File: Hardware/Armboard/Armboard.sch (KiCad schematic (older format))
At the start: 12 parts

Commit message: H-Bridge completed
Completed the H-Bridge Hierarchal Sheet
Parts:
- Conn? (x12): symbol Armboard-rescue:AndersonPP-MRDT_Connectors-Armboard-rescue -> Armboard-rescue:AndersonPP-MRDT_Connectors-Armboard-rescue-Armboard-rescue
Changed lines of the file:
@@
 $EndSheet
 $Comp
-L Armboard-rescue:AndersonPP-MRDT_Connectors-Armboard-rescue Conn?
+L Armboard-rescue:AndersonPP-MRDT_Connectors-Armboard-rescue-Armboard-rescue Conn?
 U 3 1 5F73C0FD
 P 1140 1360
@@
 $EndComp
 $Comp
-L Armboard-rescue:AndersonPP-MRDT_Connectors-Armboard-rescue Conn?
+L Armboard-rescue:AndersonPP-MRDT_Connectors-Armboard-rescue-Armboard-rescue Conn?
 U 1 1 5F73C109
 P 1140 2660
@@
 $EndComp
 $Comp
-L Armboard-rescue:AndersonPP-MRDT_Connectors-Armboard-rescue Conn?
+L Armboard-rescue:AndersonPP-MRDT_Connectors-Armboard-rescue-Armboard-rescue Conn?
 U 3 1 5F73C10F
 P 1740 1360
@@
 $EndComp
 $Comp
-L Armboard-rescue:AndersonPP-MRDT_Connectors-Armboard-rescue Conn?
+L Armboard-rescue:AndersonPP-MRDT_Connectors-Armboard-rescue-Armboard-rescue Conn?
 U 1 1 5F73C11B
 P 1740 2660
@@
 $EndComp
 $Comp
-L Armboard-rescue:AndersonPP-MRDT_Connectors-Armboard-rescue Conn?
+L Armboard-rescue:AndersonPP-MRDT_Connectors-Armboard-rescue-Armboard-rescue Conn?
 U 3 1 5F73C121
 P 2340 1360
@@
 $EndComp
 $Comp
-L Armboard-rescue:AndersonPP-MRDT_Connectors-Armboard-rescue Conn?
+L Armboard-rescue:AndersonPP-MRDT_Connectors-Armboard-rescue-Armboard-rescue Conn?
 U 1 1 5F73C12D
 P 2340 2660
@@
 $EndComp
 $Comp
-L Armboard-rescue:AndersonPP-MRDT_Connectors-Armboard-rescue Conn?
+L Armboard-rescue:AndersonPP-MRDT_Connectors-Armboard-rescue-Armboard-rescue Conn?
 U 3 1 5F73C133
 P 2940 1360
@@
 $EndComp
 $Comp
-L Armboard-rescue:AndersonPP-MRDT_Connectors-Armboard-rescue Conn?
+L Armboard-rescue:AndersonPP-MRDT_Connectors-Armboard-rescue-Armboard-rescue Conn?
 U 1 1 5F73C13F
 P 2940 2660
@@
 Anderson_Connectors
 $Comp
-L Armboard-rescue:AndersonPP-MRDT_Connectors-Armboard-rescue Conn?
+L Armboard-rescue:AndersonPP-MRDT_Connectors-Armboard-rescue-Armboard-rescue Conn?
 U 3 1 5F742E9A
 P 1140 2010
@@
 $EndComp
 $Comp
-L Armboard-rescue:AndersonPP-MRDT_Connectors-Armboard-rescue Conn?
+L Armboard-rescue:AndersonPP-MRDT_Connectors-Armboard-rescue-Armboard-rescue Conn?
 U 3 1 5F742EA0
 P 1740 2010
@@
 $EndComp
 $Comp
-L Armboard-rescue:AndersonPP-MRDT_Connectors-Armboard-rescue Conn?
+L Armboard-rescue:AndersonPP-MRDT_Connectors-Armboard-rescue-Armboard-rescue Conn?
 U 3 1 5F742EA6
 P 2340 2010
@@
 $EndComp
 $Comp
-L Armboard-rescue:AndersonPP-MRDT_Connectors-Armboard-rescue Conn?
+L Armboard-rescue:AndersonPP-MRDT_Connectors-Armboard-rescue-Armboard-rescue Conn?
 U 3 1 5F742EAC
 P 2940 2010

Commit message: Added serial pins, limit switches, titles, and indicators
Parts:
- removed Conn? (x10): AndersonPP, symbol Armboard-rescue:AndersonPP-MRDT_Connectors-Armboard-rescue-Armboard-rescue
- Conn? (x2): symbol Armboard-rescue:AndersonPP-MRDT_Connectors-Armboard-rescue-Armboard-rescue -> Armboard-rescue:AndersonPP-MRDT_Connectors-Armboard-rescue-Armboard-rescue-Armboard-rescue
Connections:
- net labels removed: +12VA, Anderson_Connectors
- wire segments 28 -> 5
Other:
- note added: "Input Andersons"

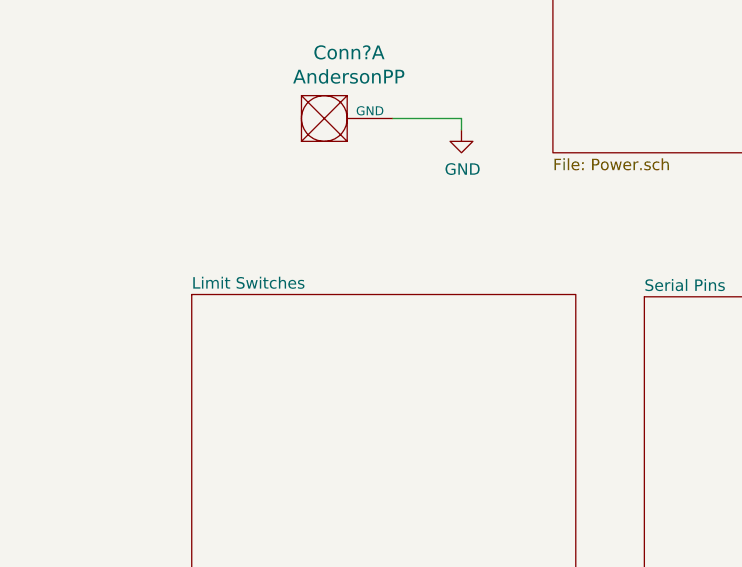
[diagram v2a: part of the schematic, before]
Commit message: Formatted GNDs and added motor toggle buttons
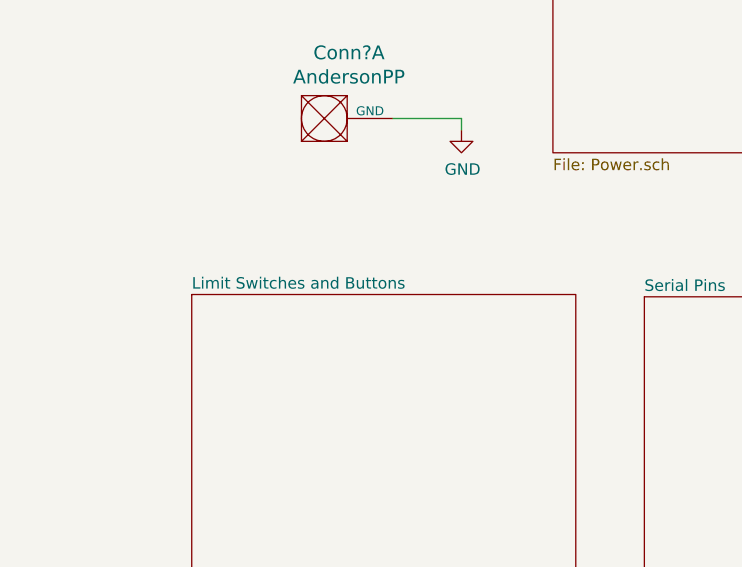
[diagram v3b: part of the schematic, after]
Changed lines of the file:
@@
 S 1520 3340 1680 1860
 U 5F739ECE
-F0 "Limit Switches" 50
+F0 "Limit Switches and Buttons" 50
 F1 "Armboard07.sch" 50
 $EndSheet

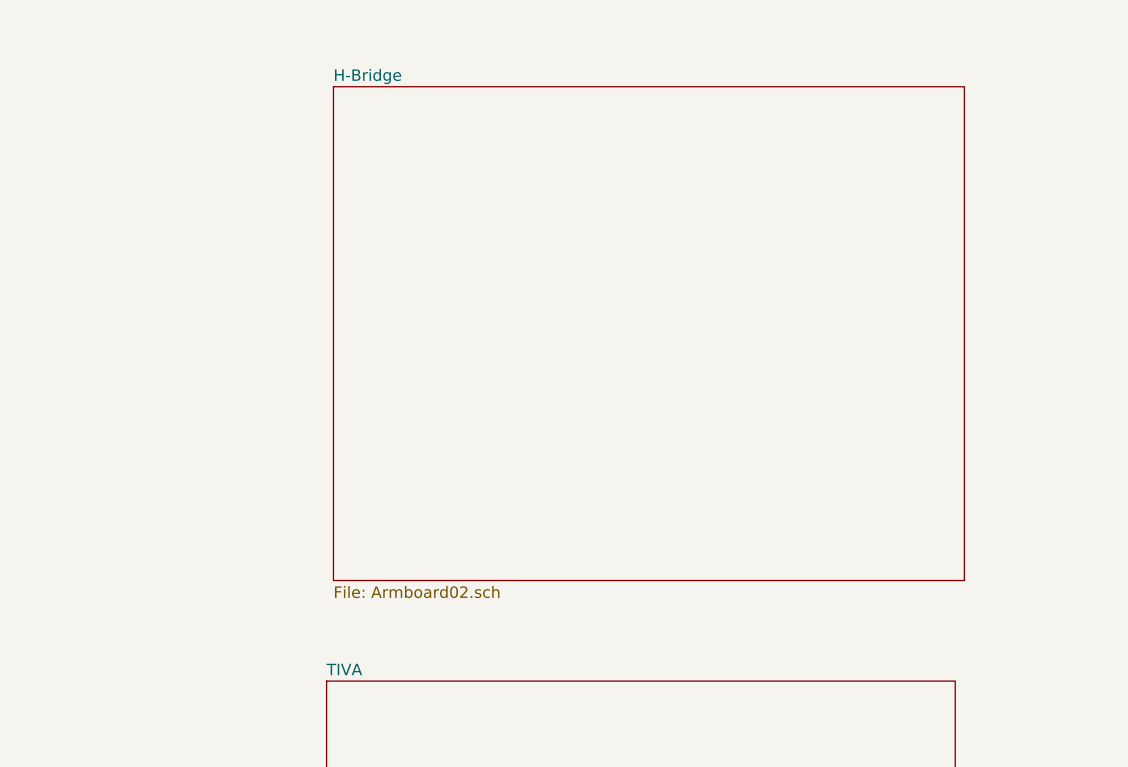
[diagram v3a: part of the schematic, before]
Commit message: Updated H-Bridge
Made the appropriate changes suggested by anthony in slack chat regarding the H-Bridge's flaws
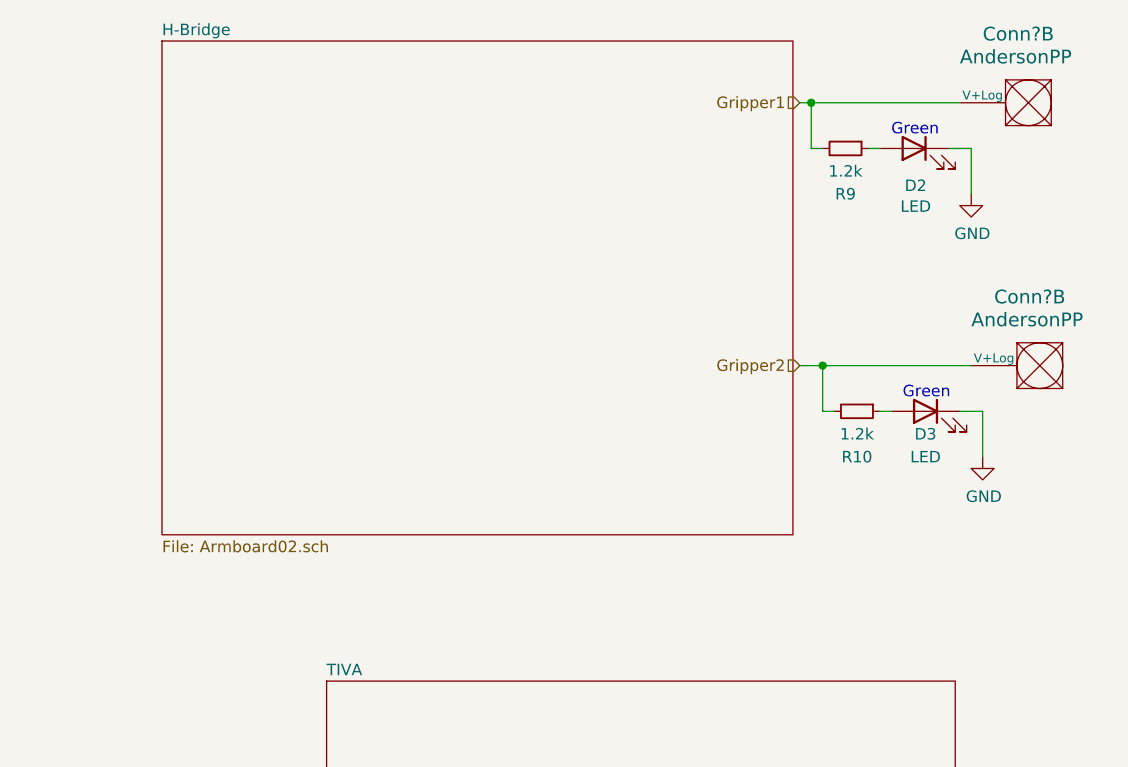
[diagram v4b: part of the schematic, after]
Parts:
- added Conn? (x2): AndersonPP, symbol MRDT_Connectors:AndersonPP
- added D2, D3: LED, symbol Device:LED
- added R10, R9: 1.2k, symbol Device:R_Small
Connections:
- net GND: now also D2.1 (K), D3.1 (K)
- new net: D2.2 (A), R9.1
- new net: D3.2 (A), R10.1
- new net Gripper1: Conn?.2 (V+Log), R9.2
- new net Gripper2: Conn?.2 (V+Log), R10.2
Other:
- note added: "Green"
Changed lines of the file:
@@
 	4900 1920 4900 1120
 $Sheet
-S 6860 1180 2760 2160
+S 6110 980  2760 2160
 U 5F7381FC
 F0 "H-Bridge" 50
@@
 Text Notes 1700 1370 0    79   ~ 16
 Input Andersons
+Text HLabel 8900 1250 0    50   Input ~ 0
+Gripper1
+Wire Wire Line
+	8900 1250 8950 1250
+Wire Wire Line
+	8950 1450 9000 1450
+$Comp
+L Device:R_Small R9
+U 1 1 5F8623A9
+P 9100 1450
+F 0 "R9" V 9300 1450 50  0000 C CNN
+F 1 "1.2k" V 9200 1450 50  0000 C CNN
+F 2 "" H 9100 1450 50  0001 C CNN
+F 3 "~" H 9100 1450 50  0001 C CNN
+	1    9100 1450
+	0    1    1    0
+$EndComp
+$Comp
+L Device:LED D2
+U 1 1 5F862E5D
+P 9400 1450
+F 0 "D2" H 9393 1287 50  0000 C CNN
+F 1 "LED" H 9393 1196 50  0000 C CNN
+F 2 "" H 9400 1450 50  0001 C CNN
+F 3 "~" H 9400 1450 50  0001 C CNN
+	1    9400 1450
+	-1   0    0    -1
+$EndComp
+Wire Wire Line
+	9250 1450 9200 1450
+Wire Wire Line
+	9550 1450 9650 1450
+$Comp
+L power:GND #PWR?
+U 1 1 5F863B11
+P 9650 1650
+F 0 "#PWR?" H 9650 1400 50  0001 C CNN
+F 1 "GND" H 9655 1477 50  0000 C CNN
+F 2 "" H 9650 1650 50  0001 C CNN
+F 3 "" H 9650 1650 50  0001 C CNN
+	1    9650 1650
+	1    0    0    -1
+$EndComp
+$Comp
+L MRDT_Connectors:AndersonPP Conn?
+U 2 1 5F864024
+P 10000 1350
+F 0 "Conn?" H 10300 1750 60  0000 R CNN
+F 1 "AndersonPP" H 10400 1650 60  0000 R CNN
+F 2 "" H 9850 800 60  0001 C CNN
+F 3 "" H 9850 800 60  0001 C CNN
+	2    10000 1350
+	-1   0    0    -1
+$EndComp
+Wire Wire Line
+	8950 1250 8950 1450
+Wire Wire Line
+	8950 1250 9600 1250
+Connection ~ 8950 1250
+Wire Wire Line
+	9650 1450 9650 1650
+Wire Wire Line
+	9000 2600 9050 2600
+$Comp
+L Device:R_Small R10
+U 1 1 5F8695AA
+P 9150 2600
+F 0 "R10" V 9350 2600 50  0000 C CNN
+F 1 "1.2k" V 9250 2600 50  0000 C CNN
+F 2 "" H 9150 2600 50  0001 C CNN
+F 3 "~" H 9150 2600 50  0001 C CNN
+	1    9150 2600
+	0    1    1    0
+$EndComp
+$Comp
+L Device:LED D3
+U 1 1 5F8695B0
+P 9450 2600
+F 0 "D3" H 9450 2500 50  0000 C CNN
+F 1 "LED" H 9450 2400 50  0000 C CNN
+F 2 "" H 9450 2600 50  0001 C CNN
+F 3 "~" H 9450 2600 50  0001 C CNN
+	1    9450 2600
+	-1   0    0    -1
+$EndComp
+Wire Wire Line
+	9300 2600 9250 2600
+Wire Wire Line
+	9600 2600 9700 2600
+$Comp
+L power:GND #PWR?
+U 1 1 5F8695B8
+P 9700 2800
+F 0 "#PWR?" H 9700 2550 50  0001 C CNN
+F 1 "GND" H 9705 2627 50  0000 C CNN
+F 2 "" H 9700 2800 50  0001 C CNN
+F 3 "" H 9700 2800 50  0001 C CNN
+	1    9700 2800
+	1    0    0    -1
+$EndComp
+$Comp
+L MRDT_Connectors:AndersonPP Conn?
+U 2 1 5F8695BE
+P 10050 2500
+F 0 "Conn?" H 10350 2900 60  0000 R CNN
+F 1 "AndersonPP" H 10450 2800 60  0000 R CNN
+F 2 "" H 9900 1950 60  0001 C CNN
+F 3 "" H 9900 1950 60  0001 C CNN
+	2    10050 2500
+	-1   0    0    -1
+$EndComp
+Wire Wire Line
+	9000 2400 9000 2600
+Wire Wire Line
+	9000 2400 9650 2400
+Connection ~ 9000 2400
+Wire Wire Line
+	9700 2600 9700 2800
+Text HLabel 8900 2400 0    50   Input ~ 0
+Gripper2
+Wire Wire Line
+	8900 2400 9000 2400
+Text Notes 9300 1400 0    50   ~ 0
+Green
+Text Notes 9350 2550 0    50   ~ 0
+Green
 $EndSCHEMATC

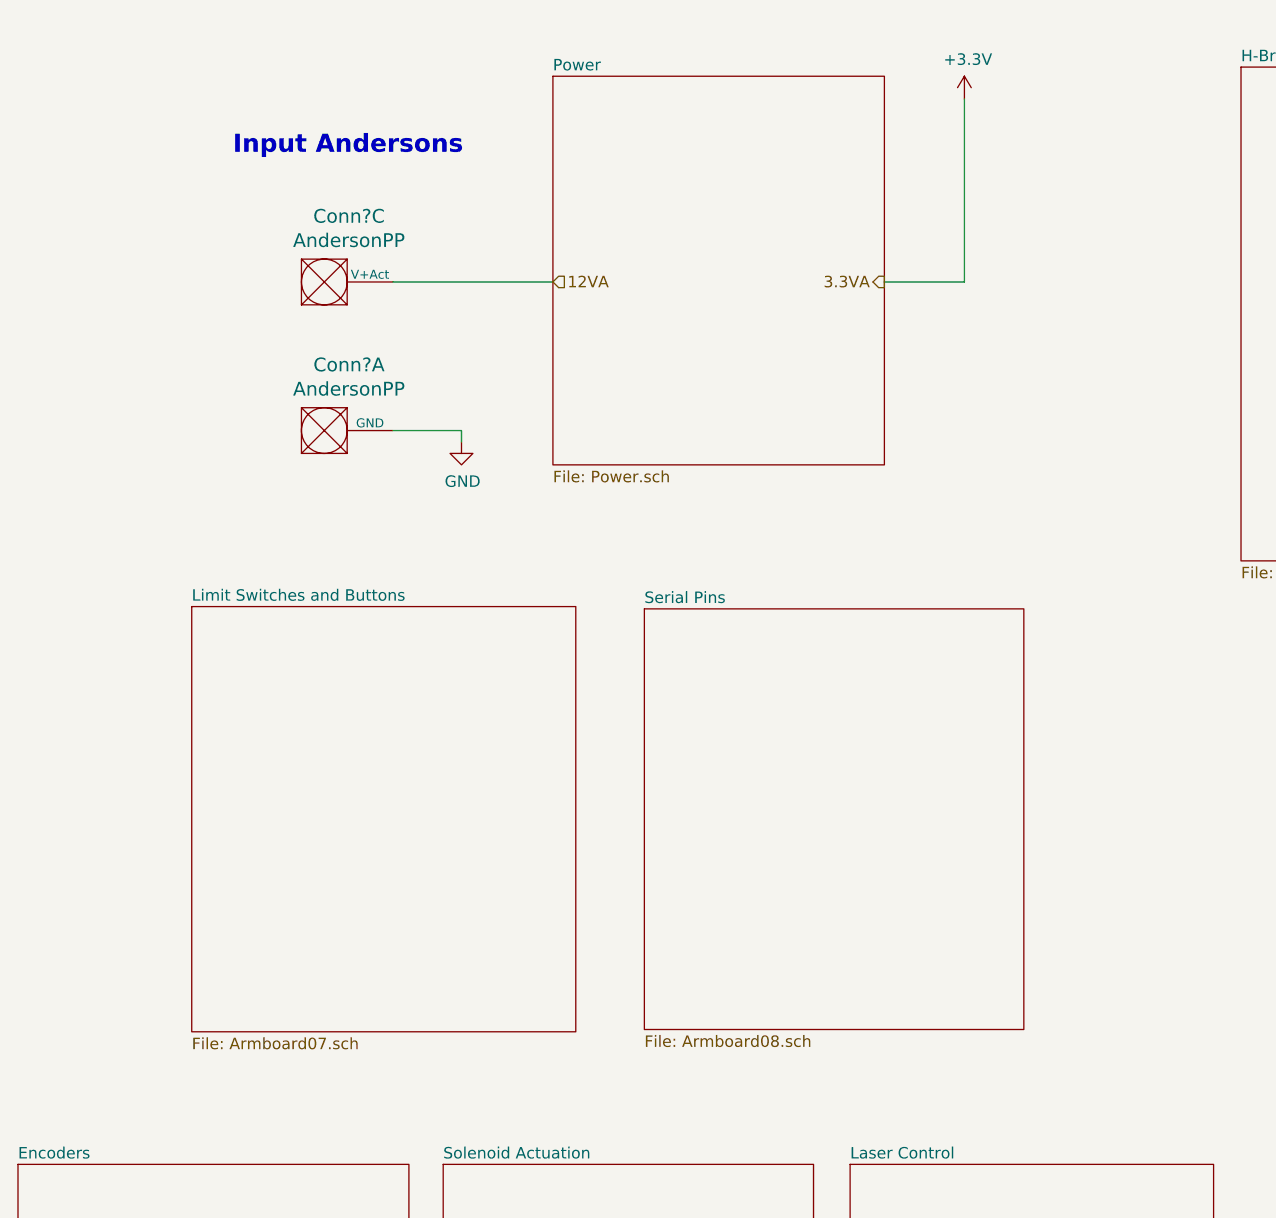
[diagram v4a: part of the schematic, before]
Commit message: Moved I/O outside of Power block
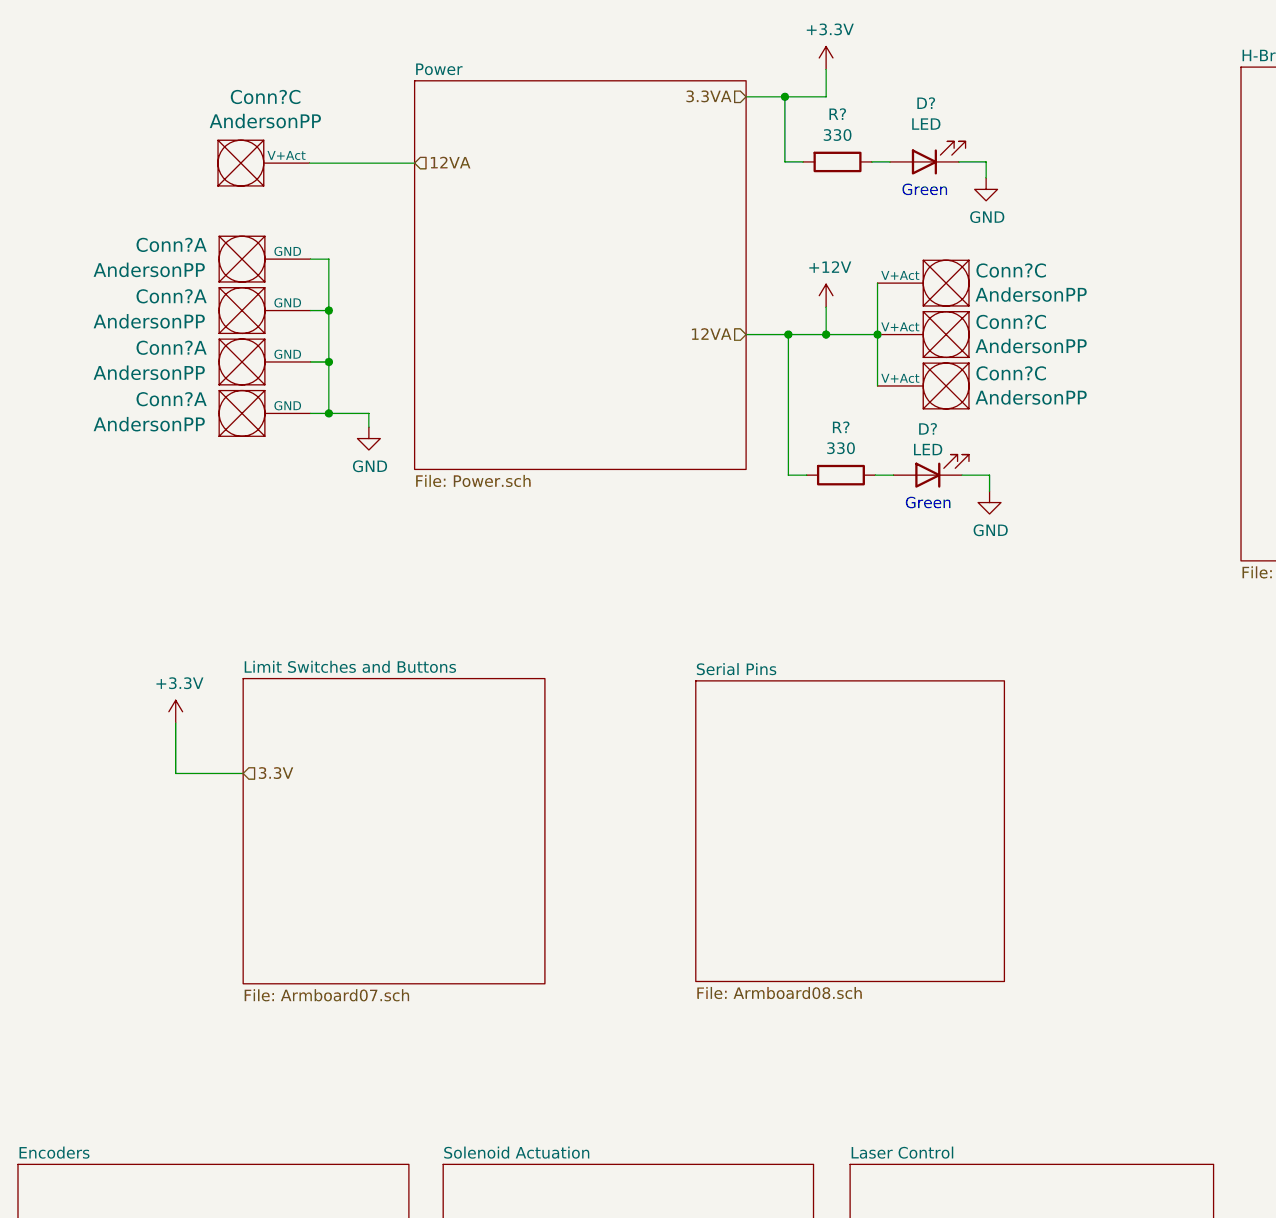
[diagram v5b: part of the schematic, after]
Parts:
- removed Conn?: AndersonPP, symbol Armboard-rescue:AndersonPP-MRDT_Connectors-Armboard-rescue-Armboard-rescue-Armb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
- added Conn? (x7): AndersonPP, symbol MRDT_Connectors:AndersonPP
- added D? (x2): LED, symbol Device:LED
- added R? (x2): 330, symbol Device:R
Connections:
- net +3V3: now also R?.2
- net GND: now also Conn?.1 (GND), Conn?.1 (GND), Conn?.1 (GND), Conn?.1 (GND), D?.1 (K), D?.1 (K)
- net 12VA renamed +12V
- net +12V: now also Conn?.3 (V+Act), Conn?.3 (V+Act), Conn?.3 (V+Act), R?.2
- new net: D?.2 (A), R?.1 (x2)
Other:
- note removed: "Input Andersons"
- moved on the sheet: Conn?C

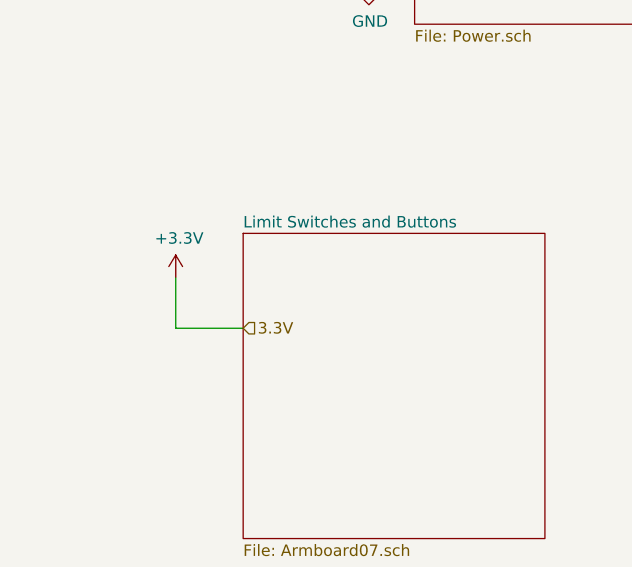
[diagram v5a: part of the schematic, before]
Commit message: Fixed buttons/switches page, changed resistor values, fixed some tiva connections
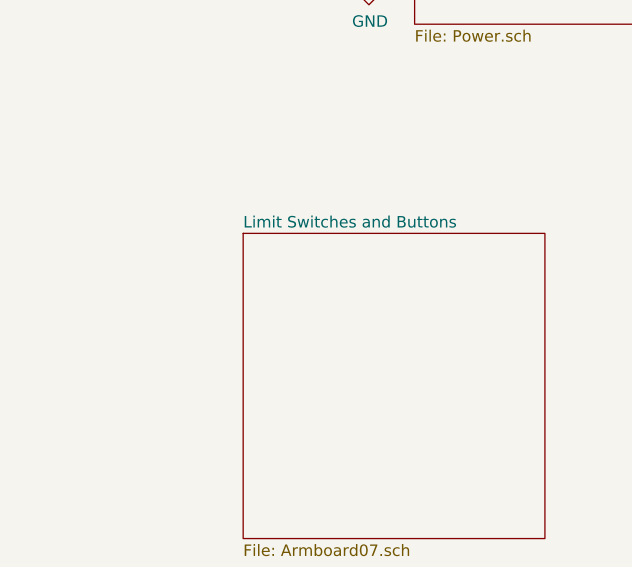
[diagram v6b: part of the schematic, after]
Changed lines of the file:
@@
 Wire Wire Line
 	2120 2045 2120 2270
-Text HLabel 1745 4070 2    50   Input ~ 0
-3.3V
-$Comp
-L power:+3.3V #PWR?
-U 1 1 5F8D31F6
-P 1450 3850
-AR Path="/5F67ABAC/5F8D31F6" Ref="#PWR?"  Part="1"
-AR Path="/5F8D31F6" Ref="#PWR?"  Part="1"
-F 0 "#PWR?" H 1450 3700 50  0001 C CNN
-F 1 "+3.3V" H 1465 4023 50  0000 C CNN
-F 2 "" H 1450 3850 50  0001 C CNN
-F 3 "" H 1450 3850 50  0001 C CNN
-	1    1450 3850
-	1    0    0    -1
-$EndComp
-Wire Wire Line
-	1745 4070 1450 4070
-Wire Wire Line
-	1450 3850 1450 4070
 $EndSCHEMATC
